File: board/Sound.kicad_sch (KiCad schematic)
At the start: 8 parts, among them J27 SND CT1/2, U57 YM2151, U58 YM3012, U59 TL074

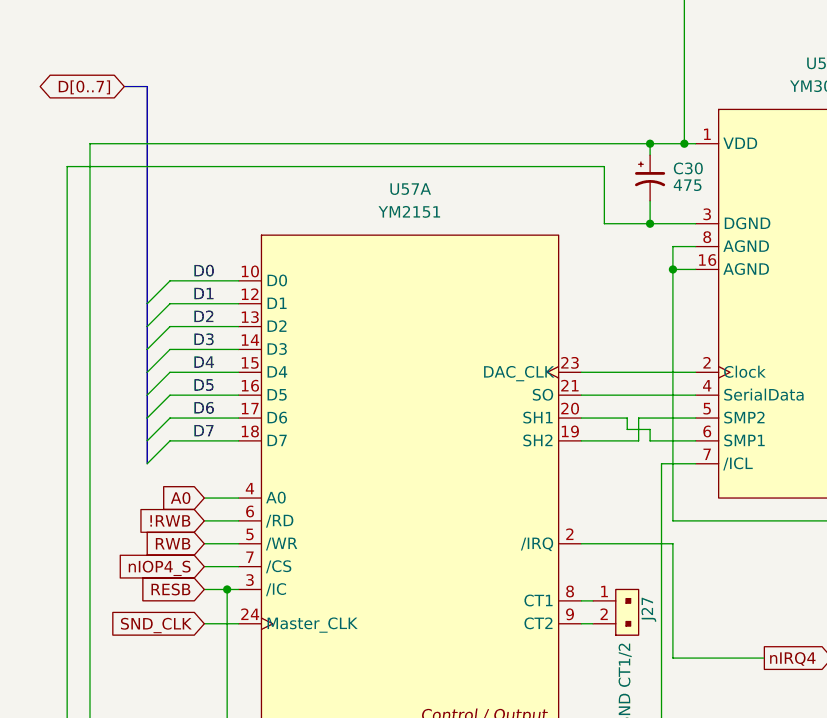
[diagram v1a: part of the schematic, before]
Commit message: V2.0 rev 2.0D: clock stretching, OS ROM paging and review fixes
Bus timing:
- New GAL C (U88) generates PHI2/PHI1 and the 3.58 MHz sound clock from
  the 14.318 MHz master, replacing the U35 74F191 divider. J36 now selects
  7.16 or 3.58 MHz.
- Banked RAM, banked ROM and slot I/O ($FF20-$FFEF) get one extra PHI2-low
  period plus 0-3 extra PHI2-high periods set in $FFF5 (GAL D). This
  replaces the on-board RDY wait generator; cards can still pull RDY.
- Write strobes are now hold-time safe: PHI1 comes straight from GAL C
  and RWB_M straight from GAL B2.

Review fixes:
- OS ROM chip enable from a single-level decode, output enable from
  GAL B1; -55 part specified. Full 4K OS ROM paging via GAL G.
- Vector RAM writes only during PHI2; $FFF0-$FFFF no longer slowed.
- YM2151 /WR on RWB_M. U62 removed. RB0-RB7 pull-ups (RN5).
- Slot clocks driven through U56 and U34 with 33R series resistors.
- J38 enables in-system flashing of the banked ROMs.
- W65C22S/W65C51N, AS6C4008, DS1813-5 and CY7C192-25 values; R4 1k.
- J7 pin 8 no longer +5V; +5VA renamed +5VSB; serial handshake loop.
- Sheet titles and revisions, slot symbol pin fixes, and project symbol
  and footprint libraries so the project opens on another machine.

Co-Authored-By: Claude Opus 5.5 <noreply@anthropic.com>
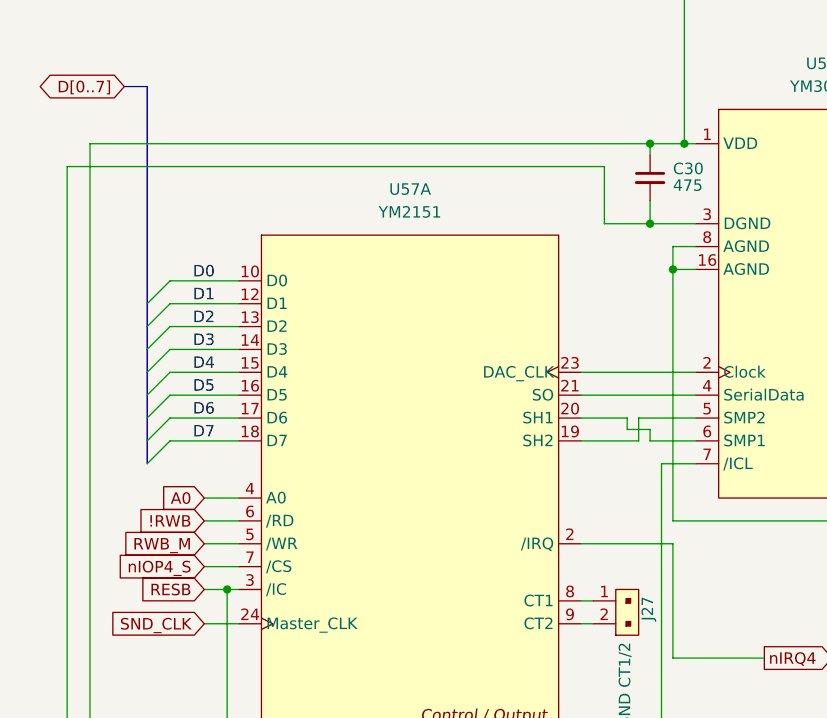
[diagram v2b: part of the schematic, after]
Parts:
- C30: symbol Device:C_Polarized_Small_US -> Device:C_Small
- J27: symbol dk_Rectangular-Connectors-Headers-Male-Pins:22-23-2021 -> Hydra16:22-23-2021_1
- U57: symbol Yamaha 2151-3012:YM2151 -> Hydra16:YM2151
- U58: symbol Yamaha 2151-3012:YM3012 -> Hydra16:YM3012
- U59: symbol dk_Linear-Amplifiers-Instrumentation-OP-Amps-Buffer-Amps:TL074CN -> Hydra16:TL074CN
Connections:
- net RWB renamed RWB_M
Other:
- title: ZeroPage $00/$01 Mirror Memory and RAM/ROM Bank Logic -> Sound (YM2151 / YM3012)
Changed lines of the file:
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@@
 	(paper "A4")
 	(title_block
-		(title "ZeroPage $00/$01 Mirror Memory and RAM/ROM Bank Logic")
-		(date "2026-01-28")
-		(rev "2.0B")
+		(title "Sound (YM2151 / YM3012)")
+		(date "2026-10-06")
+		(rev "2.0D")
 		(company "Data Tuning")
 		(comment 1 "Hydra 16")
@@
 		)
 	)
-	(global_label "RWB"
+	(global_label "RWB_M"
 		(shape input)
 		(at 72.39 118.11 180)
@@
 	)
 	(symbol
-		(lib_id "dk_Linear-Amplifiers-Instrumentation-OP-Amps-Buffer-Amps:TL074CN")
+		(lib_id "Hydra16:TL074CN")
 		(at 200.66 95.25 0)
 		(unit 4)
@@
 	)
 	(symbol
-		(lib_id "dk_Linear-Amplifiers-Instrumentation-OP-Amps-Buffer-Amps:TL074CN")
+		(lib_id "Hydra16:TL074CN")
 		(at 176.53 74.93 0)
 		(unit 1)
@@
 	)
 	(symbol
-		(lib_id "Yamaha 2151-3012:YM3012")
+		(lib_id "Hydra16:YM3012")
 		(at 127 109.22 0)
 		(unit 1)
@@
 	)
 	(symbol
-		(lib_id "dk_Linear-Amplifiers-Instrumentation-OP-Amps-Buffer-Amps:TL074CN")
+		(lib_id "Hydra16:TL074CN")
 		(at 200.66 74.93 0)
 		(unit 2)
@@
 	)
 	(symbol
-		(lib_id "Device:C_Polarized_Small_US")
+		(lib_id "Device:C_Small")
 		(at 121.92 77.47 0)
 		(unit 1)
@@
 	)
 	(symbol
-		(lib_name "22-23-2021_1")
-		(lib_id "dk_Rectangular-Connectors-Headers-Male-Pins:22-23-2021")
+		(lib_id "Hydra16:22-23-2021_1")
 		(at 118.11 127 90)
 		(unit 1)
@@
 	)
 	(symbol
-		(lib_id "Yamaha 2151-3012:YM2151")
+		(lib_id "Hydra16:YM2151")
 		(at 76.2 137.16 0)
 		(unit 1)
@@
 	)
 	(symbol
-		(lib_id "Yamaha 2151-3012:YM2151")
+		(lib_id "Hydra16:YM2151")
 		(at 77.47 198.12 0)
 		(unit 2)
@@
 	)
 	(symbol
-		(lib_id "dk_Linear-Amplifiers-Instrumentation-OP-Amps-Buffer-Amps:TL074CN")
+		(lib_id "Hydra16:TL074CN")
 		(at 176.53 106.68 0)
 		(unit 3)

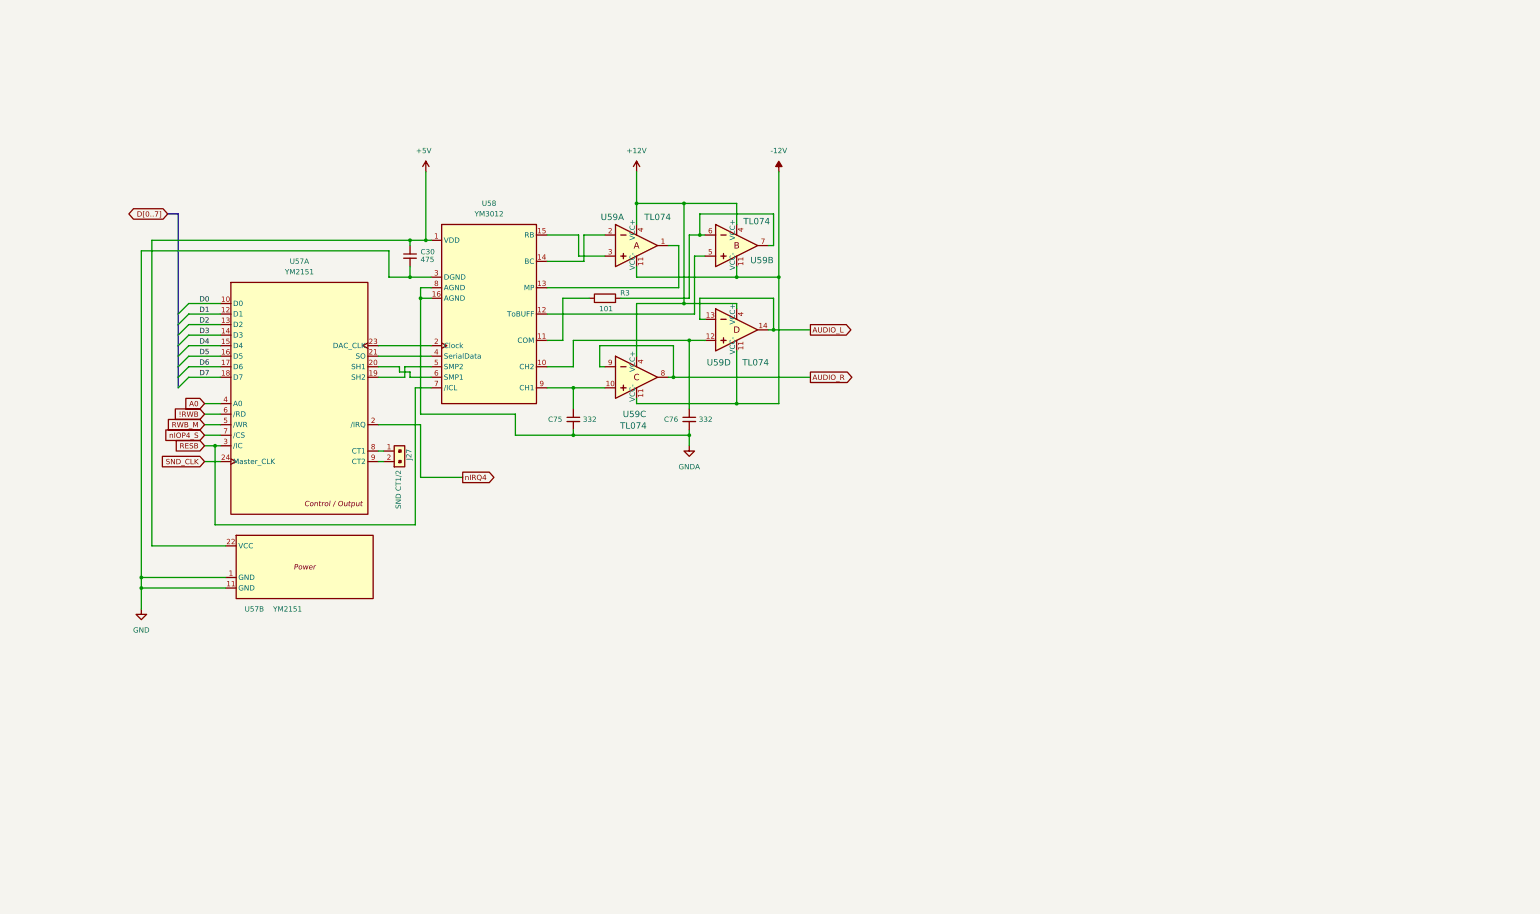
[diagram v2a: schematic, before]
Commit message: V2.0: split Support sheet, add stereo amplifier and on-board speakers
Support sheet reorganized (connectivity unchanged):
- Support.kicad_sch renamed to Power: ATX, front panel, reset, soft power, -5V
- Oscillators and their parts moved to Clocks (now US Ledger)
- Sound-chip decoupling and line-out parts moved to Sound
- VIA CB1/CB2/SPI pull-ups moved to Connectors
- Also includes minor schematic edits made before the reorganization

Audio output rework (Sound, now A3):
- U89 TDA2822M stereo amplifier on 9 V from U90 L7809 (fed by +12V)
- RV1 dual 10k log volume pot behind R26/R27 220k attenuators
- J18 moved from Connectors and now uses the switched TRS symbol:
  a plug lifts T/R off TN/RN and mutes the on-board speakers
- LS1/LS2 8 ohm mini speakers through R30/R31 (15R 0.5 W)
- New footprint Speaker_D32mm_P15.24mm_P17.50mm (two pad pairs, fits
  Adafruit 1898 or Kitronik 3316)
- J39 line-out header (LINE_L, LINE_R, GNDA)
- R18 stays the single GNDA-GND tie, to sit at U89 pin 4
- TDA2822M symbol added to hydra16.kicad_sym

Co-Authored-By: Claude Opus 5.5 <noreply@anthropic.com>
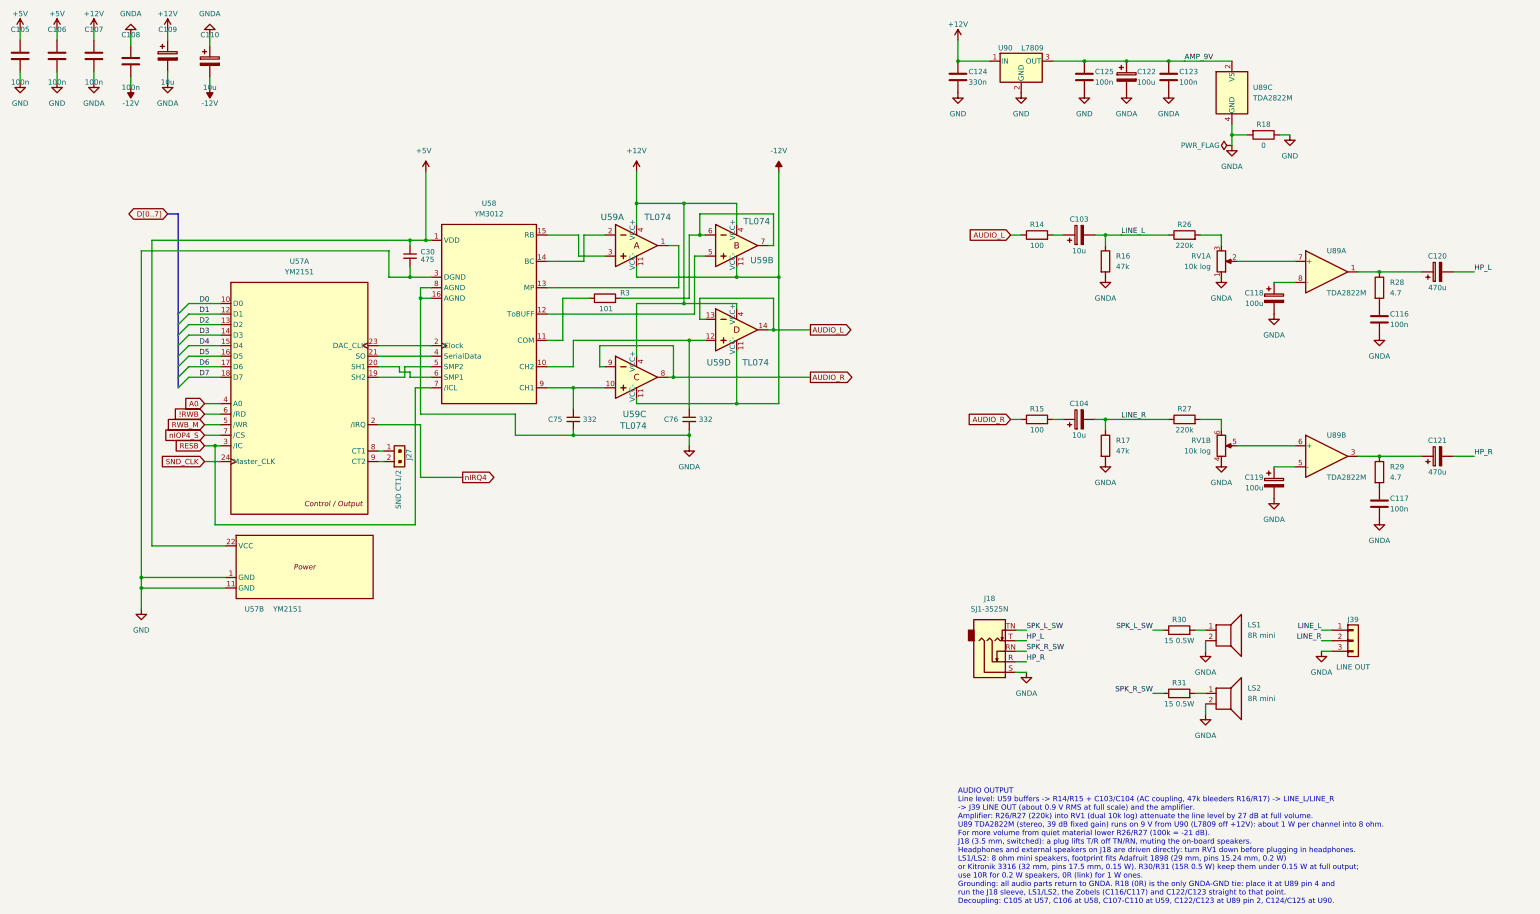
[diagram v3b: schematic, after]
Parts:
- added C103, C104, C109, C110: 10u, Capacitor_THT:CP_Radial_D5.0mm_P2.00mm, symbol Device:C_Polarized
- added C105, C106, C107, C108, C116, C117, C123, C125: 100n, Capacitor_THT:C_Disc_D5.0mm_W2.5mm_P5.00mm, symbol Device:C
- added C118, C119, C122: 100u, Capacitor_THT:CP_Radial_D6.3mm_P2.50mm, symbol Device:C_Polarized
- added C120, C121: 470u, Capacitor_THT:CP_Radial_D8.0mm_P3.50mm, symbol Device:C_Polarized
- added C124: 330n, Capacitor_THT:C_Disc_D5.0mm_W2.5mm_P5.00mm, symbol Device:C
- added J18: SJ1-3525N, Connector_Audio:Jack_3.5mm_CUI_SJ1-3525N_Horizontal, symbol Connector_Audio:AudioJack3_SwitchTR
- added J39: LINE OUT, Connector_PinHeader_2.54mm:PinHeader_1x03_P2.54mm_Vertical, symbol Connector_Generic:Conn_01x03
- added LS1, LS2: 8R mini, Hydra16:Speaker_D32mm_P15.24mm_P17.50mm, symbol Device:Speaker
- added R14, R15: 100, Resistor_THT:R_Axial_DIN0204_L3.6mm_D1.6mm_P5.08mm_Horizontal, symbol Device:R
- added R16, R17: 47k, Resistor_THT:R_Axial_DIN0204_L3.6mm_D1.6mm_P5.08mm_Horizontal, symbol Device:R
- added R18: 0, Resistor_THT:R_Axial_DIN0204_L3.6mm_D1.6mm_P5.08mm_Horizontal, symbol Device:R
- added R26, R27: 220k, Resistor_THT:R_Axial_DIN0204_L3.6mm_D1.6mm_P5.08mm_Horizontal, symbol Device:R
- added R28, R29: 4.7, Resistor_THT:R_Axial_DIN0204_L3.6mm_D1.6mm_P5.08mm_Horizontal, symbol Device:R
- added R30, R31: 15 0.5W, Resistor_THT:R_Axial_DIN0207_L6.3mm_D2.5mm_P10.16mm_Horizontal, symbol Device:R
- added RV1: 10k log, Potentiometer_THT:Potentiometer_Alps_RK097_Dual_Horizontal, symbol Device:R_Potentiometer_Dual_Separate
- added U89: TDA2822M, Package_DIP:DIP-8_W7.62mm_Socket_LongPads, symbol Hydra16:TDA2822M
- added U90: L7809, Package_TO_SOT_THT:TO-220-3_Vertical, symbol Regulator_Linear:L7809
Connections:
- net +12V: now also C107.1, C109.1, C124.1, U90.1 (IN)
- net +5V: now also C105.1, C106.1
- net -12V: now also C108.2, C110.2
- net AUDIO_L: now also R14.1
- net AUDIO_R: now also R15.1
- net GND: now also C105.2, C106.2, C124.2, C125.2, R18.1, U90.2 (GND)
- net GNDA: now also C107.2, C108.1, C109.2, C110.1, C116.2, C117.2, C118.2, C119.2, C122.2, C123.2, J18.S, J39.3 (Pin_3), LS1.2, LS2.2, R16.2, R17.2, R18.2, RV1.1, RV1.4, U89.4 (GND)
- new net: C117.1, R29.2
- new net: C104.1, R15.2
- new net: C121.1, R29.1, U89.3
- new net: R26.2, RV1.3
- new net: C120.1, R28.1, U89.1
- new net: RV1.2, U89.7 (+)
- new net: C118.1, U89.8 (-)
- new net: C103.1, R14.2
- new net: RV1.5, U89.6 (+)
- new net: R27.2, RV1.6
- new net: LS1.1, R30.2
- new net: C119.1, U89.5 (-)
- new net: LS2.1, R31.2
- new net: C116.1, R28.2
- new net AMP_9V: C122.1, C123.1, C125.1, U89.2 (VS), U90.3 (OUT)
- new net HP_L: C120.2, J18.T
- new net HP_R: C121.2, J18.R
- new net LINE_L: C103.2, J39.1 (Pin_1), R16.1, R26.1
- new net LINE_R: C104.2, J39.2 (Pin_2), R17.1, R27.1
- new net SPK_L_SW: J18.TN, R30.1
- new net SPK_R_SW: J18.RN, R31.1
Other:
- note added: "AUDIO OUTPUT Line level: U59 buffers -> R14/R15 + C103/C104 (AC coupling, 47k bleeders R16/R17) -> LINE_L/LINE_R -> J39 LINE OUT (about 0.9 V RMS at full scale) and the amplifier. Amplifier: R26/R27 (220k) into RV1 (dual 10k log) attenuate the line level by 27 dB at full volume. U89 TDA2822M (stereo, 39 dB fixed gain) runs on 9 V from U90 (L7809 off +12V): about 1 W per channel into 8 ohm. For mo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"
- title: Sound (YM2151 / YM3012) -> Sound: YM2151 / YM3012, Line Out, Amplifier and Speakers

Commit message: V2.0: slot pin 9 to +3.3V, amplifier on +5V
Slots:
- Pin 9 on all six slots now carries +3.3V instead of -5V, so each card
  gets two 3.3 V pins (9 and 24); no existing card used -5V
- Slot connector symbol pin 9 renamed +3.3V; slot bus rules note updated
- Removed U80 (79L05), C98 and C99 from the Power sheet

Amplifier:
- U89 TDA2822M now runs from +5V through an RC filter (R32 1R, C122 1000u)
- Removed U90 (L7809), C124 and C125
- R26/R27 470k (same volume range at 5 V); R30/R31 2.2R (same footprint)
- PWR_FLAG on the new AMP_5V net; sheet note updated

PCB updated from the schematic.

Also tidied overlapping text on the Power sheet (U78/U79 labels, PWR_FLAG,
R19/C111/R20/C112); connectivity unchanged.

Co-Authored-By: Claude Opus 5.5 <noreply@anthropic.com>
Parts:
- removed C124: 330n, Capacitor_THT:C_Disc_D5.0mm_W2.5mm_P5.00mm, symbol Device:C
- removed C125: 100n, Capacitor_THT:C_Disc_D5.0mm_W2.5mm_P5.00mm, symbol Device:C
- removed U90: L7809, Package_TO_SOT_THT:TO-220-3_Vertical, symbol Regulator_Linear:L7809
- added R32: 1, Resistor_THT:R_Axial_DIN0204_L3.6mm_D1.6mm_P5.08mm_Horizontal, symbol Device:R
- C122: value 100u -> 1000u; footprint Capacitor_THT:CP_Radial_D6.3mm_P2.50mm -> Capacitor_THT:CP_Radial_D10.0mm_P5.00mm
- R26, R27: value 220k -> 470k
- R30, R31: value 15 0.5W -> 2.2
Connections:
- net +5V: now also R32.1
- net AMP_9V renamed AMP_5V
- net AMP_5V: now also R32.2
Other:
- note added: "AUDIO OUTPUT Line level: U59 buffers -> R14/R15 + C103/C104 (AC coupling, 47k bleeders R16/R17) -> LINE_L/LINE_R -> J39 LINE OUT (about 0.9 V RMS at full scale) and the amplifier. Amplifier: R26/R27 (470k) into RV1 (dual 10k log) attenuate the line level by 34 dB at full volume. U89 TDA2822M (stereo, 39 dB fixed gain) runs from +5V through R32/C122 (1R + 1000u, a 160 Hz filter that keeps logic no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"
- note removed: "AUDIO OUTPUT Line level: U59 buffers -> R14/R15 + C103/C104 (AC coupling, 47k bleeders R16/R17) -> LINE_L/LINE_R -> J39 LINE OUT (about 0.9 V RMS at full scale) and the amplifier. Amplifier: R26/R27 (220k) into RV1 (dual 10k log) attenuate the line level by 27 dB at full volume. U89 TDA2822M (stereo, 39 dB fixed gain) runs on 9 V from U90 (L7809 off +12V): about 1 W per channel into 8 ohm. For mo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"
